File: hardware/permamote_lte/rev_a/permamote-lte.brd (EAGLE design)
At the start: 27 x 60 mm, 116 parts, among them J1 DM3AT-SF-PEJM5, J2 NANO_SIM, J3 TC2030-JLINK-NL, J4 U.FL-R-SMT, J5 U.FL-R-SMT, Q1 PMDXB950UPEL, Q2 PMDXB950UPEL, Q3 PMDXB950UPEL, Q4 PMDXB950UPEL, Q5 PMDXB950UPEL, Q6 PMDXB950UPEL, Q7 PMDXB950UPEL, Q8 PMDXB950UPEL, Q9 PMDXB950UPEL, U1 AB1815-T3, U10 SI7021-A20-GM1, U11 SIP32510, U12 TCS34725, U13 TPD3F303DPVR, U2 BGA725L6, U3 BQ25505, U4 EKMB1101111, U5 LIS2DW12, U6 MAX17222, U7 MAX44009, U8 MS5637-02BA03, U9 NRF9160, X1 ABS07-32.768KHZ-7-T

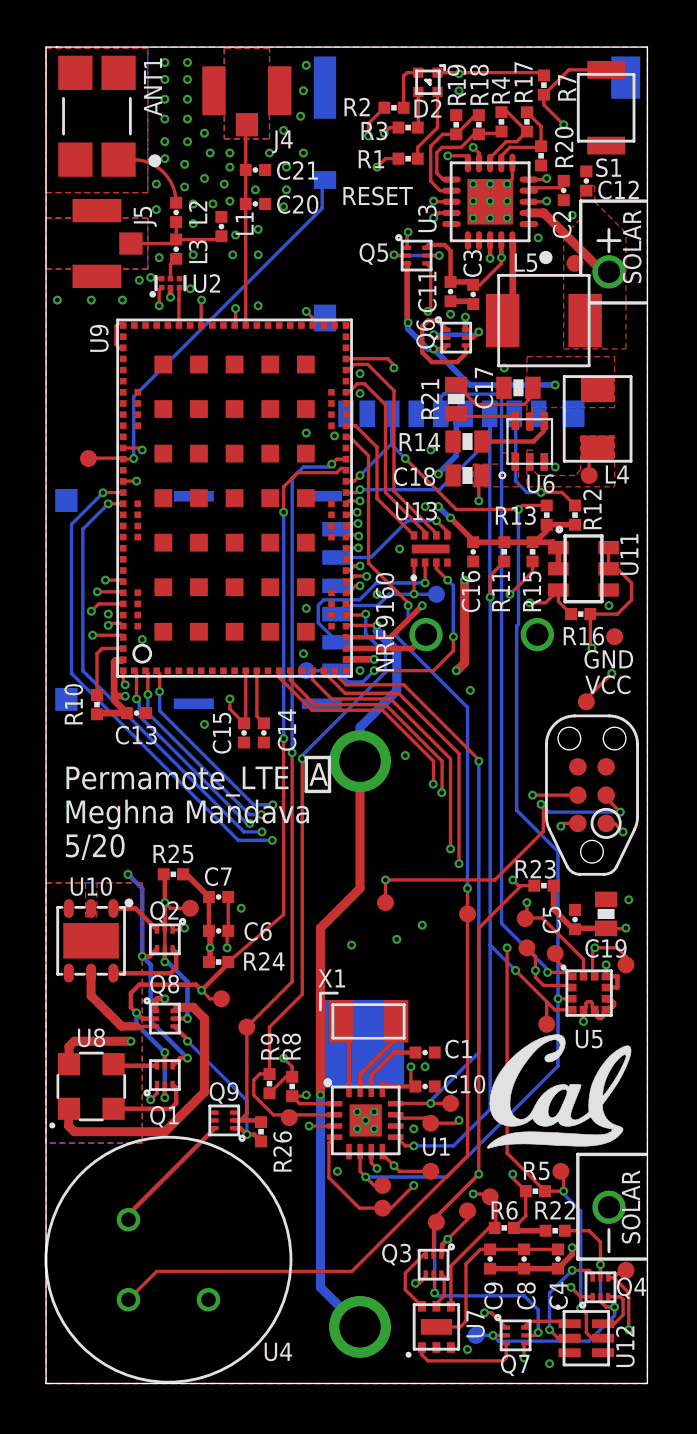
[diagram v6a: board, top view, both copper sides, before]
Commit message: holes arent covered anymore
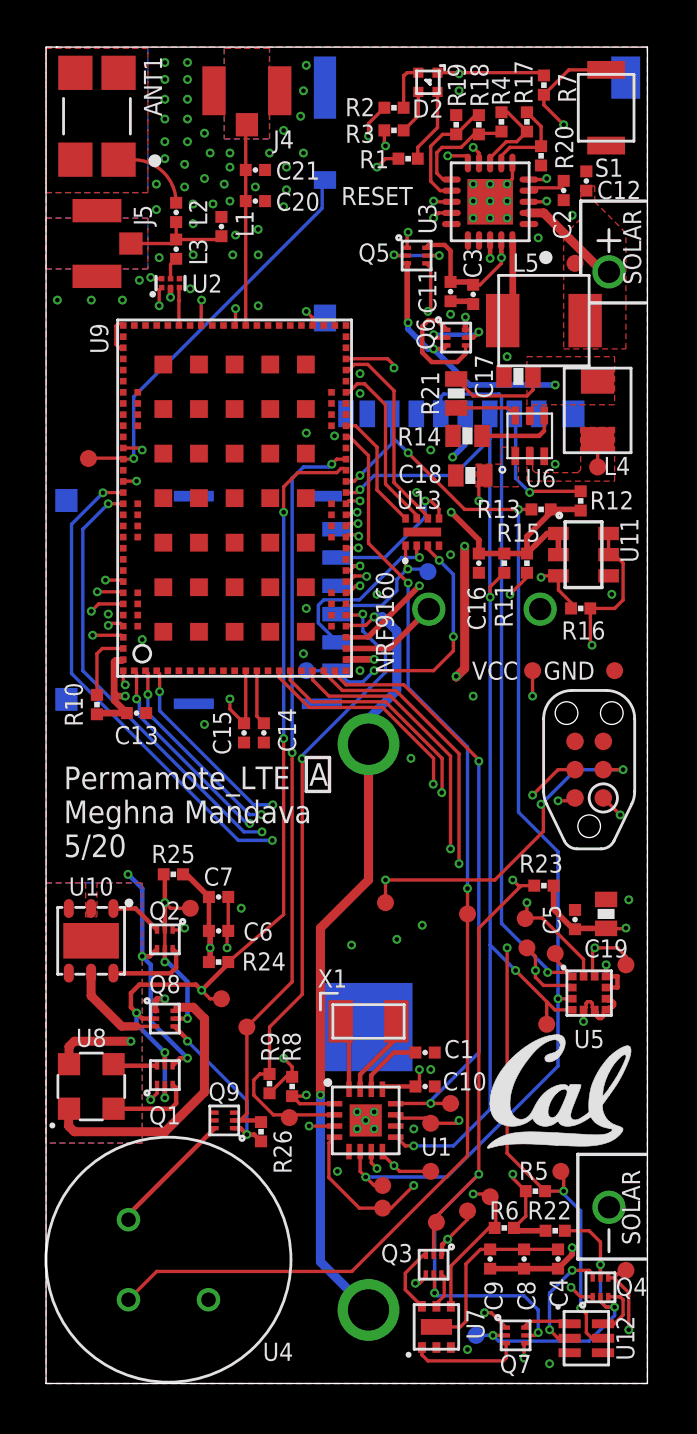
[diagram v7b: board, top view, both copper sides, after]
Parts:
- moved TP25 2.79 mm to (21.8, 32.0)
- moved TP26 1.52 mm to (25.5, 32.0)
- moved BT1 1.15 mm to (19.7, 34.8)
- moved J3 1.15 mm to (24.4, 27.6)
- moved TP27 1.09 mm to (17.1, 36.4)
- moved BT2 0.85 mm to (14.5, 16.0)
- moved U13 0.85 mm to (16.9, 38.2)
- moved R12 0.68 mm to (24.0, 39.6)
- moved R3 0.65 mm to (15.6, 56.3)
- moved U11 0.63 mm to (24.1, 37.2)
- moved C16 0.57 mm to (19.4, 36.8)
- moved R15 0.57 mm to (21.6, 36.8)
- moved TP24 0.54 mm to (24.8, 41.1)
- moved C17 0.51 mm to (21.2, 45.2)
- moved R11 0.51 mm to (20.6, 36.8)
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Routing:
- net N$13: track 14.4 -> 15.7 mm, vias 3 -> 2
- net SWDIO: track 20.1 -> 19.0 mm
- net MISO: track 53.1 -> 52.0 mm
- net SIM_RST: track 6.44 -> 5.52 mm
- net SIM_IO2: track 11.7 -> 12.6 mm
- net SIM_IO: track 10.0 -> 9.12 mm
- net SIM_CLK: track 8.93 -> 8.01 mm
- net !SD_DETECT: track 42.1 -> 41.4 mm
- net LED_BLUE: track 22.7 -> 22.1 mm
- net VCC: track 65.4 -> 64.7 mm
- net VSEC: track 22.7 -> 22.1 mm
- net SD_ENABLE: track 25.9 -> 26.4 mm
- net PIR_OUT: track 53.1 -> 52.5 mm
- net MOSI: track 52.7 -> 52.2 mm
